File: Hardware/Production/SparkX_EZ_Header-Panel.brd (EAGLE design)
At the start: 187.2 x 136.7 mm, 1386 parts, among them J1 QWIIC_RIGHT_ANGLE, J10 QWIIC_RIGHT_ANGLE, J11 QWIIC_RIGHT_ANGLE, J12 QWIIC_RIGHT_ANGLE, J13 QWIIC_RIGHT_ANGLE, J14 QWIIC_RIGHT_ANGLE, J15 QWIIC_RIGHT_ANGLE, J16 QWIIC_RIGHT_ANGLE, J17 QWIIC_RIGHT_ANGLE, J18 QWIIC_RIGHT_ANGLE, J19 QWIIC_RIGHT_ANGLE, J2 QWIIC_RIGHT_ANGLE, J20 QWIIC_RIGHT_ANGLE, J21 QWIIC_RIGHT_ANGLE, J22 QWIIC_RIGHT_ANGLE, J23 QWIIC_RIGHT_ANGLE, J24 QWIIC_RIGHT_ANGLE, J25 QWIIC_RIGHT_ANGLE, J26 QWIIC_RIGHT_ANGLE, J27 QWIIC_RIGHT_ANGLE, J28 QWIIC_RIGHT_ANGLE, J29 QWIIC_RIGHT_ANGLE, J3 QWIIC_RIGHT_ANGLE, J30 QWIIC_RIGHT_ANGLE, J4 QWIIC_RIGHT_ANGLE, J5 QWIIC_RIGHT_ANGLE, J6 QWIIC_RIGHT_ANGLE, J7 QWIIC_RIGHT_ANGLE, J8 QWIIC_RIGHT_ANGLE, J9 QWIIC_RIGHT_ANGLE

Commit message: Add bottom silk
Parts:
- added LOGO31, LOGO32, LOGO34, LOGO35, LOGO37, LOGO38, LOGO40, LOGO41, LOGO43, LOGO44, LOGO46, LOGO47, LOGO49, LOGO50, LOGO52, LOGO53, LOGO55, LOGO56, LOGO58, LOGO59, LOGO61, LOGO62, LOGO64, LOGO65, LOGO67, LOGO68, LOGO70, LOGO71, LOGO73, LOGO74, LOGO76, LOGO77, LOGO79, LOGO80, LOGO82, LOGO83, LOGO85, LOGO86, LOGO88, LOGO89: OSHW-LOGOMINI, SparkFun-Aesthetics:OSHW-LOGO-MINI
- added LOGO33, LOGO36, LOGO39, LOGO42, LOGO45, LOGO48, LOGO51, LOGO54, LOGO57, LOGO60, LOGO63, LOGO66, LOGO69, LOGO72, LOGO75, LOGO78, LOGO81, LOGO84, LOGO87, LOGO90: QWIIC_LOGO_5MM, SparkFun-Aesthetics:QWIIC_5MM
- added U$1000, U$1019, U$1038, U$1057, U$1076, U$1095, U$1114, U$1133, U$601, U$620, U$639, U$658, U$677, U$696, U$715, U$734, U$753, U$772, U$791, U$810, U$829, U$848, U$867, U$886, U$905, U$924, U$943, U$962, U$981: (no value), output:#CIPO#0
- added U$1001, U$1020, U$1039, U$1058, U$1077, U$1096, U$1115, U$1134, U$602, U$621, U$640, U$659, U$678, U$697, U$716, U$735, U$754, U$773, U$792, U$811, U$830, U$849, U$868, U$887, U$906, U$925, U$944, U$963, U$982: (no value), output:#GPIO1#0
- added U$1002, U$1021, U$1040, U$1059, U$1078, U$1097, U$1116, U$1135, U$603, U$622, U$641, U$660, U$679, U$698, U$717, U$736, U$755, U$774, U$793, U$812, U$831, U$850, U$869, U$888, U$907, U$926, U$945, U$964, U$983: (no value), output:#CS0#0
- added U$1003, U$1022, U$1041, U$1060, U$1079, U$1098, U$1117, U$1136, U$604, U$623, U$642, U$661, U$680, U$699, U$718, U$737, U$756, U$775, U$794, U$813, U$832, U$851, U$870, U$889, U$908, U$927, U$946, U$965, U$984: (no value), output:#GPIO0#0
- added U$1004, U$1023, U$1042, U$1061, U$1080, U$1099, U$1118, U$1137, U$605, U$624, U$643, U$662, U$681, U$700, U$719, U$738, U$757, U$776, U$795, U$814, U$833, U$852, U$871, U$890, U$909, U$928, U$947, U$966, U$985: (no value), output:#CS1#0
- added U$1005, U$1024, U$1043, U$1062, U$1081, U$1100, U$1119, U$1138, U$606, U$625, U$644, U$663, U$682, U$701, U$720, U$739, U$758, U$777, U$796, U$815, U$834, U$853, U$872, U$891, U$910, U$929, U$948, U$967, U$986: (no value), output:#CS2#0
- added U$1006, U$1044, U$1082, U$1120, U$626, U$664, U$702, U$740, U$778, U$816, U$854, U$892, U$930, U$968: (no value), output:#I�C#0
- added U$1007, U$1025, U$1045, U$1063, U$1083, U$1101, U$1121, U$1139, U$607, U$627, U$645, U$665, U$683, U$703, U$721, U$741, U$759, U$779, U$797, U$817, U$835, U$855, U$873, U$893, U$911, U$931, U$949, U$969, U$987: (no value), output:EZ_HEADER0
- added U$1008, U$1026, U$1046, U$1064, U$1084, U$1102, U$1122, U$1140, U$608, U$628, U$646, U$666, U$684, U$704, U$722, U$742, U$760, U$780, U$798, U$818, U$836, U$856, U$874, U$894, U$912, U$932, U$950, U$970, U$988: (no value), output:#SCL#0
- added U$1009, U$1027, U$1047, U$1065, U$1085, U$1103, U$1123, U$609, U$629, U$647, U$667, U$685, U$705, U$723, U$743, U$761, U$781, U$799, U$819, U$837, U$857, U$875, U$895, U$913, U$933, U$951, U$971, U$989: SPARKX-LOGO3, SparkX:SPARKX-SMALL
- added U$1010, U$1029, U$1048, U$1067, U$1086, U$1105, U$1124, U$611, U$630, U$649, U$668, U$687, U$706, U$725, U$744, U$763, U$782, U$801, U$820, U$839, U$858, U$877, U$896, U$915, U$934, U$953, U$972, U$991: (no value), output:#V_USB#0
- added U$1011, U$1012, U$1030, U$1031, U$1049, U$1050, U$1068, U$1069, U$1087, U$1088, U$1106, U$1107, U$1125, U$1126, U$612, U$613, U$631, U$632, U$650, U$651, U$669, U$670, U$688, U$689, U$707, U$708, U$726, U$727, U$745, U$746, U$764, U$765, U$783, U$784, U$802, U$803, U$821, U$822, U$840, U$841, U$859, U$860, U$878, U$879, U$897, U$898, U$916, U$917, U$935, U$936, U$954, U$955, U$973, U$974, U$992, U$993: (no value), output:#3#3V#0
- added U$1013, U$1032, U$1051, U$1070, U$1089, U$1108, U$1127, U$614, U$633, U$652, U$671, U$690, U$709, U$728, U$747, U$766, U$785, U$804, U$823, U$842, U$861, U$880, U$899, U$918, U$937, U$956, U$975, U$994: (no value), output:#PWR_EN#0
- added U$1014, U$1015, U$1033, U$1034, U$1052, U$1053, U$1071, U$1072, U$1090, U$1091, U$1109, U$1110, U$1128, U$1129, U$615, U$616, U$634, U$635, U$653, U$654, U$672, U$673, U$691, U$692, U$710, U$711, U$729, U$730, U$748, U$749, U$767, U$768, U$786, U$787, U$805, U$806, U$824, U$825, U$843, U$844, U$862, U$863, U$881, U$882, U$900, U$901, U$919, U$920, U$938, U$939, U$957, U$958, U$976, U$977, U$995, U$996: (no value), output:#GND#0
- added U$1016, U$1035, U$1054, U$1073, U$1092, U$1111, U$1130, U$617, U$636, U$655, U$674, U$693, U$712, U$731, U$750, U$769, U$788, U$807, U$826, U$845, U$864, U$883, U$902, U$921, U$940, U$959, U$978, U$997: (no value), output:#SCLK#0
- added U$1017, U$1036, U$1055, U$1074, U$1093, U$1112, U$1131, U$618, U$637, U$656, U$675, U$694, U$713, U$732, U$751, U$770, U$789, U$808, U$827, U$846, U$865, U$884, U$903, U$922, U$941, U$960, U$979, U$998: (no value), output:#COPI#0
- added U$1018, U$1037, U$1056, U$1075, U$1094, U$1113, U$1132, U$619, U$638, U$657, U$676, U$695, U$714, U$733, U$752, U$771, U$790, U$809, U$828, U$847, U$866, U$885, U$904, U$923, U$942, U$961, U$980, U$999: (no value), output:#SDA#0
- added U$1028, U$1066, U$1104, U$610, U$648, U$686, U$724, U$762, U$800, U$838, U$876, U$914, U$952, U$990: (no value), output:#OUT#0
- LOGO12, LOGO15, LOGO18, LOGO21, LOGO24, LOGO27, LOGO30, LOGO4, LOGO6, LOGO9: value OSHW-LOGOMINI -> QWIIC_LOGO_5MM; device SparkFun-Aesthetics:OSHW-LOGO-MINI -> SparkFun-Aesthetics:QWIIC_5MM
- U$100, U$460, U$480, U$80: device output:#SCL#0 -> output:#3#3V#0
- U$101, U$481: value SPARKX-LOGO3 -> (none); device SparkX:SPARKX-SMALL -> output:#PWR_EN#0
- U$102, U$122, U$482, U$502: device output:#OUT#0 -> output:#GND#0
- U$103, U$463, U$483, U$83: device output:#V_USB#0 -> output:#GND#0
- U$104, U$465, U$484, U$85: device output:#3#3V#0 -> output:#SCLK#0
- U$105, U$124, U$485, U$504: device output:#3#3V#0 -> output:#COPI#0
- U$106, U$486: device output:#PWR_EN#0 -> output:#SDA#0
- U$107, U$468, U$487, U$88: device output:#GND#0 -> output:#CIPO#0
- U$108, U$127, U$488, U$507: device output:#GND#0 -> output:#GPIO1#0
- U$109, U$489: device output:#SCLK#0 -> output:#CS0#0
- U$110, U$490: device output:#COPI#0 -> output:#GPIO0#0
- U$111, U$491: device output:#SDA#0 -> output:#CS1#0
- U$112, U$492: device output:#CIPO#0 -> output:#CS2#0
- U$113, U$133, U$493, U$513: device output:#GPIO1#0 -> output:EZ_HEADER0
- U$114, U$134, U$494, U$514: device output:#CS0#0 -> output:#SCL#0
- U$115, U$135, U$495, U$515: value (none) -> SPARKX-LOGO3; device output:#GPIO0#0 -> SparkX:SPARKX-SMALL
- U$116, U$496: device output:#CS1#0 -> output:#OUT#0
- U$117, U$497: device output:#CS2#0 -> output:#V_USB#0
- U$118, U$138, U$498, U$518: device output:#I�C#0 -> output:#3#3V#0
- U$119, U$479, U$499, U$99: device output:EZ_HEADER0 -> output:#3#3V#0
- U$120, U$500: device output:#SCL#0 -> output:#PWR_EN#0
- U$121, U$141, U$501, U$521: value SPARKX-LOGO3 -> (none); device SparkX:SPARKX-SMALL -> output:#GND#0
- U$123, U$503: device output:#V_USB#0 -> output:#SCLK#0
- U$125, U$144, U$505, U$524: device output:#3#3V#0 -> output:#SDA#0
- U$126, U$506: device output:#PWR_EN#0 -> output:#CIPO#0
- U$128, U$147, U$508, U$527: device output:#GND#0 -> output:#CS0#0
- U$129, U$509: device output:#SCLK#0 -> output:#GPIO0#0
- U$130, U$510: device output:#COPI#0 -> output:#CS1#0
- U$131, U$511: device output:#SDA#0 -> output:#CS2#0
- U$132, U$512: device output:#CIPO#0 -> output:#I�C#0
- U$136, U$516: device output:#CS1#0 -> output:#V_USB#0
- U$137, U$157, U$517, U$537: device output:#CS2#0 -> output:#3#3V#0
- U$139, U$519: device output:EZ_HEADER0 -> output:#PWR_EN#0
- U$140, U$160, U$520, U$540: device output:#SCL#0 -> output:#GND#0
- U$142, U$522: device output:#OUT#0 -> output:#SCLK#0
- U$143, U$523: device output:#V_USB#0 -> output:#COPI#0
- U$145, U$164, U$525, U$544: device output:#3#3V#0 -> output:#CIPO#0
- U$146, U$526: device output:#PWR_EN#0 -> output:#GPIO1#0
- U$148, U$167, U$528, U$547: device output:#GND#0 -> output:#GPIO0#0
- U$149, U$529: device output:#SCLK#0 -> output:#CS1#0
- U$150, U$530: device output:#COPI#0 -> output:#CS2#0
- U$151, U$171, U$531, U$551: device output:#SDA#0 -> output:EZ_HEADER0
- U$152, U$172, U$532, U$552: device output:#CIPO#0 -> output:#SCL#0
- U$153, U$173, U$533, U$553: value (none) -> SPARKX-LOGO3; device output:#GPIO1#0 -> SparkX:SPARKX-SMALL
- U$154, U$534: device output:#CS0#0 -> output:#OUT#0
- U$155, U$535: device output:#GPIO0#0 -> output:#V_USB#0
- U$156, U$176, U$536, U$556: device output:#CS1#0 -> output:#3#3V#0
- U$158, U$538: device output:#I�C#0 -> output:#PWR_EN#0
- U$159, U$179, U$539, U$559: device output:EZ_HEADER0 -> output:#GND#0
- U$161, U$541: value SPARKX-LOGO3 -> (none); device SparkX:SPARKX-SMALL -> output:#SCLK#0
- U$162, U$542: device output:#OUT#0 -> output:#COPI#0
- U$163, U$543: device output:#V_USB#0 -> output:#SDA#0
- U$165, U$184, U$545, U$564: device output:#3#3V#0 -> output:#GPIO1#0
- U$166, U$546: device output:#PWR_EN#0 -> output:#CS0#0
- U$168, U$187, U$548, U$567: device output:#GND#0 -> output:#CS1#0
- U$169, U$549: device output:#SCLK#0 -> output:#CS2#0
- U$170, U$550: device output:#COPI#0 -> output:#I�C#0
- U$174, U$554: device output:#CS0#0 -> output:#V_USB#0
- U$175, U$195, U$555, U$575: device output:#GPIO0#0 -> output:#3#3V#0
- U$177, U$557: device output:#CS2#0 -> output:#PWR_EN#0
- U$178, U$198, U$558, U$578: device output:#I�C#0 -> output:#GND#0
- U$180, U$560: device output:#SCL#0 -> output:#SCLK#0
- U$181, U$561: value SPARKX-LOGO3 -> (none); device SparkX:SPARKX-SMALL -> output:#COPI#0
- U$182, U$562: device output:#OUT#0 -> output:#SDA#0
- U$183, U$563: device output:#V_USB#0 -> output:#CIPO#0
- U$185, U$204, U$565, U$584: device output:#3#3V#0 -> output:#CS0#0
- U$186, U$566: device output:#PWR_EN#0 -> output:#GPIO0#0
- U$188, U$207, U$568, U$587: device output:#GND#0 -> output:#CS2#0
- U$189, U$209, U$569, U$589: device output:#SCLK#0 -> output:EZ_HEADER0
- U$190, U$210, U$570, U$590: device output:#COPI#0 -> output:#SCL#0
- U$191, U$211, U$571, U$591: value (none) -> SPARKX-LOGO3; device output:#SDA#0 -> SparkX:SPARKX-SMALL
- U$192, U$572: device output:#CIPO#0 -> output:#OUT#0
- U$193, U$573: device output:#GPIO1#0 -> output:#V_USB#0
- U$194, U$214, U$574, U$594: device output:#CS0#0 -> output:#3#3V#0
- U$196, U$576: device output:#CS1#0 -> output:#PWR_EN#0
- U$197, U$217, U$577, U$597: device output:#CS2#0 -> output:#GND#0
- U$199, U$579: device output:EZ_HEADER0 -> output:#SCLK#0
- U$200, U$580: device output:#SCL#0 -> output:#COPI#0
- U$201, U$581: value SPARKX-LOGO3 -> (none); device SparkX:SPARKX-SMALL -> output:#SDA#0
- U$202, U$582: device output:#OUT#0 -> output:#CIPO#0
- U$203, U$583: device output:#V_USB#0 -> output:#GPIO1#0
- U$205, U$224, U$585: device output:#3#3V#0 -> output:#GPIO0#0
- U$206, U$586: device output:#PWR_EN#0 -> output:#CS1#0
- U$208, U$588: device output:#GND#0 -> output:#I�C#0
- U$212, U$592: device output:#CIPO#0 -> output:#V_USB#0
- U$213, U$233, U$593: device output:#GPIO1#0 -> output:#3#3V#0
- U$215, U$595: device output:#GPIO0#0 -> output:#PWR_EN#0
- U$216, U$236, U$596: device output:#CS1#0 -> output:#GND#0
- U$218, U$598: device output:#I�C#0 -> output:#SCLK#0
- U$219, U$599: device output:EZ_HEADER0 -> output:#COPI#0
- U$22, U$402: device output:#OUT#0 -> output:#V_USB#0
- U$220, U$600: device output:#SCL#0 -> output:#SDA#0
- U$221: value SPARKX-LOGO3 -> (none); device SparkX:SPARKX-SMALL -> output:#CIPO#0
- U$222: device output:#OUT#0 -> output:#GPIO1#0
- U$223: device output:#V_USB#0 -> output:#CS0#0
- U$225, U$244: device output:#3#3V#0 -> output:#CS1#0
- U$226: device output:#PWR_EN#0 -> output:#CS2#0
- U$227, U$247: device output:#GND#0 -> output:EZ_HEADER0
- U$228, U$248: device output:#GND#0 -> output:#SCL#0
- U$229, U$249: value (none) -> SPARKX-LOGO3; device output:#SCLK#0 -> SparkX:SPARKX-SMALL
- U$23, U$403, U$423, U$43: device output:#V_USB#0 -> output:#3#3V#0
- U$230: device output:#COPI#0 -> output:#OUT#0
- U$231: device output:#SDA#0 -> output:#V_USB#0
- U$232, U$252: device output:#CIPO#0 -> output:#3#3V#0
- U$234: device output:#CS0#0 -> output:#PWR_EN#0
- U$235, U$255: device output:#GPIO0#0 -> output:#GND#0
- U$237: device output:#CS2#0 -> output:#SCLK#0
- U$238: device output:#I�C#0 -> output:#COPI#0
- U$239: device output:EZ_HEADER0 -> output:#SDA#0
- U$240: device output:#SCL#0 -> output:#CIPO#0
- U$241: value SPARKX-LOGO3 -> (none); device SparkX:SPARKX-SMALL -> output:#GPIO1#0
- U$242: device output:#OUT#0 -> output:#CS0#0
- U$243: device output:#V_USB#0 -> output:#GPIO0#0
- U$245, U$264: device output:#3#3V#0 -> output:#CS2#0
- U$246: device output:#PWR_EN#0 -> output:#I�C#0
- U$25, U$405, U$424, U$44: device output:#3#3V#0 -> output:#PWR_EN#0
- U$250: device output:#COPI#0 -> output:#V_USB#0
- U$251, U$271: device output:#SDA#0 -> output:#3#3V#0
- U$253: device output:#GPIO1#0 -> output:#PWR_EN#0
- U$254, U$274: device output:#CS0#0 -> output:#GND#0
- U$256: device output:#CS1#0 -> output:#SCLK#0
- U$257: device output:#CS2#0 -> output:#COPI#0
- U$258: device output:#I�C#0 -> output:#SDA#0
- U$259: device output:EZ_HEADER0 -> output:#CIPO#0
- U$26, U$406, U$426, U$46: device output:#PWR_EN#0 -> output:#GND#0
- U$260: device output:#SCL#0 -> output:#GPIO1#0
- U$261: value SPARKX-LOGO3 -> (none); device SparkX:SPARKX-SMALL -> output:#CS0#0
- U$262: device output:#OUT#0 -> output:#GPIO0#0
- U$263: device output:#V_USB#0 -> output:#CS1#0
- U$265, U$285: device output:#3#3V#0 -> output:EZ_HEADER0
- U$266, U$286: device output:#PWR_EN#0 -> output:#SCL#0
- U$267, U$287: value (none) -> SPARKX-LOGO3; device output:#GND#0 -> SparkX:SPARKX-SMALL
- U$268: device output:#GND#0 -> output:#OUT#0
- U$269: device output:#SCLK#0 -> output:#V_USB#0
- U$270, U$290: device output:#COPI#0 -> output:#3#3V#0
- U$272: device output:#CIPO#0 -> output:#PWR_EN#0
- U$273, U$293: device output:#GPIO1#0 -> output:#GND#0
- U$275: device output:#GPIO0#0 -> output:#SCLK#0
- U$276: device output:#CS1#0 -> output:#COPI#0
- U$277: device output:#CS2#0 -> output:#SDA#0
- U$278: device output:#I�C#0 -> output:#CIPO#0
- U$279: device output:EZ_HEADER0 -> output:#GPIO1#0
- U$28, U$408, U$427, U$47: device output:#GND#0 -> output:#SCLK#0
- U$280: device output:#SCL#0 -> output:#CS0#0
- U$281: value SPARKX-LOGO3 -> (none); device SparkX:SPARKX-SMALL -> output:#GPIO0#0
- U$282: device output:#OUT#0 -> output:#CS1#0
- U$283: device output:#V_USB#0 -> output:#CS2#0
- U$284: device output:#3#3V#0 -> output:#I�C#0
- U$288, U$307: device output:#GND#0 -> output:#V_USB#0
- U$289, U$309: device output:#SCLK#0 -> output:#3#3V#0
- U$29, U$409: device output:#SCLK#0 -> output:#COPI#0
- U$291: device output:#SDA#0 -> output:#PWR_EN#0
- U$292, U$312: device output:#CIPO#0 -> output:#GND#0
- U$294: device output:#CS0#0 -> output:#SCLK#0
- U$295: device output:#GPIO0#0 -> output:#COPI#0
- U$296: device output:#CS1#0 -> output:#SDA#0
- U$297: device output:#CS2#0 -> output:#CIPO#0
- U$298: device output:#I�C#0 -> output:#GPIO1#0
- U$299: device output:EZ_HEADER0 -> output:#CS0#0
- U$30, U$410: device output:#COPI#0 -> output:#SDA#0
- U$300: device output:#SCL#0 -> output:#GPIO0#0
- U$301: value SPARKX-LOGO3 -> (none); device SparkX:SPARKX-SMALL -> output:#CS1#0
- U$302: device output:#OUT#0 -> output:#CS2#0
- U$303, U$323: device output:#V_USB#0 -> output:EZ_HEADER0
- U$304, U$324: device output:#3#3V#0 -> output:#SCL#0
- U$305, U$325: value (none) -> SPARKX-LOGO3; device output:#3#3V#0 -> SparkX:SPARKX-SMALL
- U$306: device output:#PWR_EN#0 -> output:#OUT#0
- U$308, U$327, U$328, U$347: device output:#GND#0 -> output:#3#3V#0
- U$31, U$411: device output:#SDA#0 -> output:#CIPO#0
- U$310: device output:#COPI#0 -> output:#PWR_EN#0
- U$311, U$331: device output:#SDA#0 -> output:#GND#0
- U$313: device output:#GPIO1#0 -> output:#SCLK#0
- U$314: device output:#CS0#0 -> output:#COPI#0
- U$315: device output:#GPIO0#0 -> output:#SDA#0
- U$316: device output:#CS1#0 -> output:#CIPO#0
- U$317: device output:#CS2#0 -> output:#GPIO1#0
- U$318: device output:#I�C#0 -> output:#CS0#0
- U$319: device output:EZ_HEADER0 -> output:#GPIO0#0
- U$32, U$412: device output:#CIPO#0 -> output:#GPIO1#0
- U$320: device output:#SCL#0 -> output:#CS1#0
- U$321: value SPARKX-LOGO3 -> (none); device SparkX:SPARKX-SMALL -> output:#CS2#0
- U$322: device output:#OUT#0 -> output:#I�C#0
- U$326: device output:#PWR_EN#0 -> output:#V_USB#0
- U$329: device output:#SCLK#0 -> output:#PWR_EN#0
- U$33, U$413: device output:#GPIO1#0 -> output:#CS0#0
- U$330, U$350: device output:#COPI#0 -> output:#GND#0
- U$332: device output:#CIPO#0 -> output:#SCLK#0
- U$333: device output:#GPIO1#0 -> output:#COPI#0
- U$334: device output:#CS0#0 -> output:#SDA#0
- U$335: device output:#GPIO0#0 -> output:#CIPO#0
- U$336: device output:#CS1#0 -> output:#GPIO1#0
- U$337: device output:#CS2#0 -> output:#CS0#0
- U$338: device output:#I�C#0 -> output:#GPIO0#0
- U$339: device output:EZ_HEADER0 -> output:#CS1#0
- U$34, U$414: device output:#CS0#0 -> output:#GPIO0#0
- U$340: device output:#SCL#0 -> output:#CS2#0
- U$341, U$361: value SPARKX-LOGO3 -> (none); device SparkX:SPARKX-SMALL -> output:EZ_HEADER0
- U$342, U$362: device output:#OUT#0 -> output:#SCL#0
- U$343, U$363: value (none) -> SPARKX-LOGO3; device output:#V_USB#0 -> SparkX:SPARKX-SMALL
- U$344: device output:#3#3V#0 -> output:#OUT#0
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
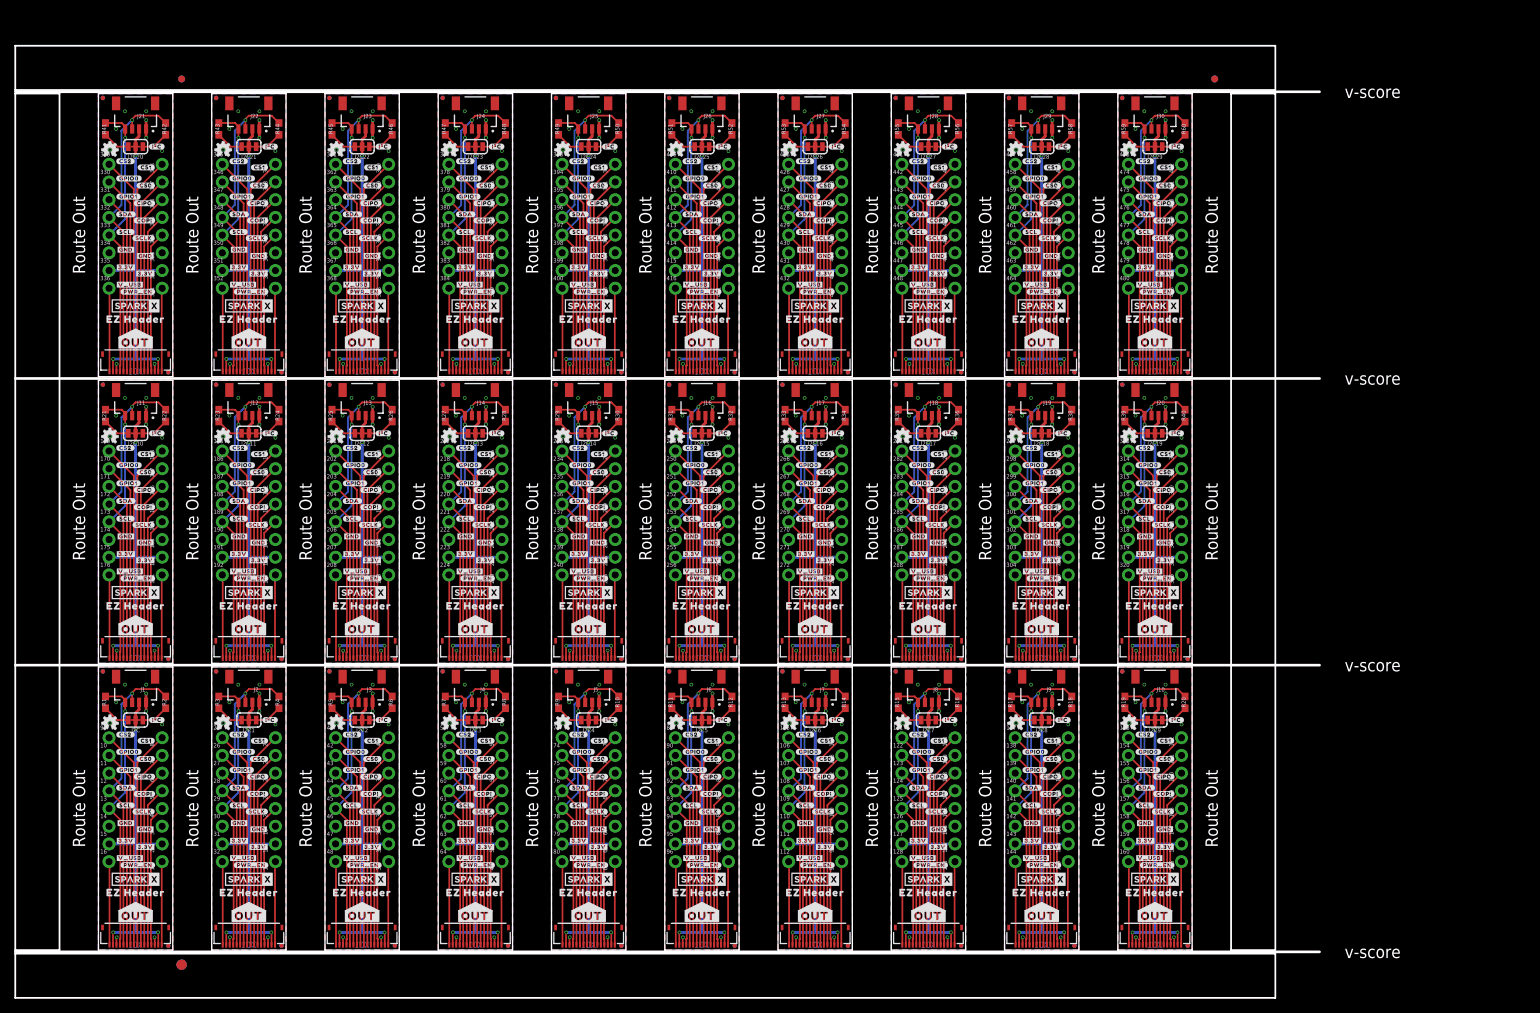
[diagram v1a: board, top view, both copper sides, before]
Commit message: Gapless production panel
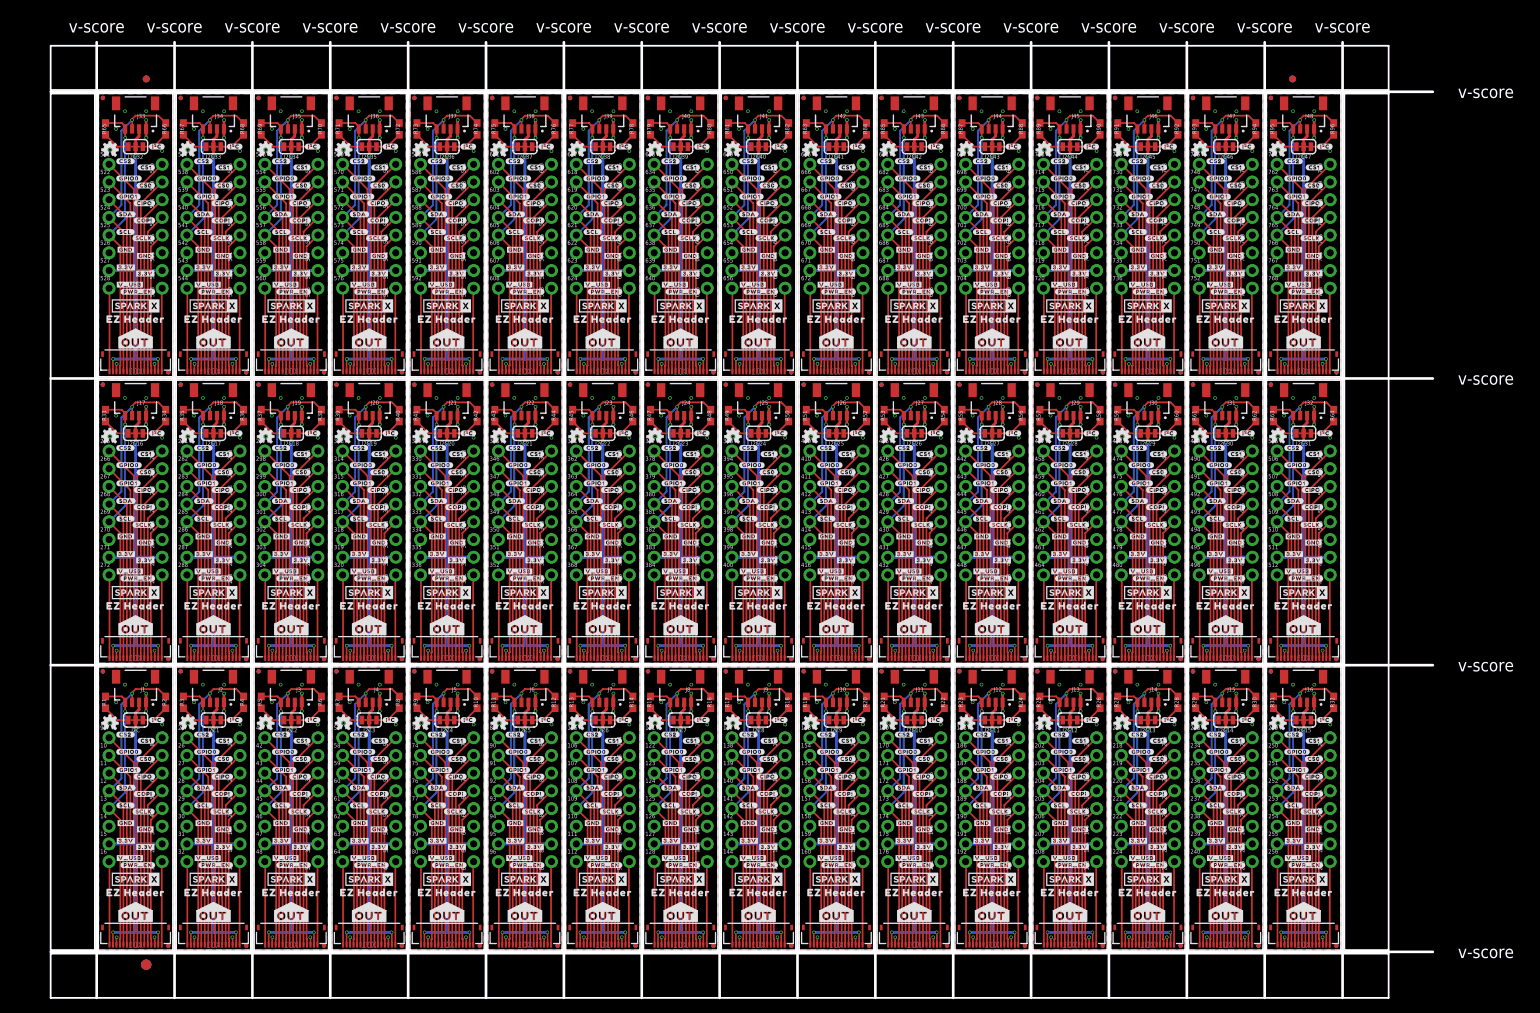
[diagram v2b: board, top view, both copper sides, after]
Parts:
- added 481, 482, 483, 484, 485, 486, 487, 488, 489, 490, 491, 492, 493, 494, 495, 496, 497, 498, 499, 500, 501, 502, 503, 504, 505, 506, 507, 508, 509, 510, 511, 512, 513, 514, 515, 516, 517, 518, 519, 520, 521, 522, 523, 524, 525, 526, 527, 528, 529, 530, 531, 532, 533, 534, 535, 536, 537, 538, 539, 540, 541, 542, 543, 544, 545, 546, 547, 548, 549, 550, 551, 552, 553, 554, 555, 556, 557, 558, 559, 560, 561, 562, 563, 564, 565, 566, 567, 568, 569, 570, 571, 572, 573, 574, 575, 576, 577, 578, 579, 580, 581, 582, 583, 584, 585, 586, 587, 588, 589, 590, 591, 592, 593, 594, 595, 596, 597, 598, 599, 600, 601, 602, 603, 604, 605, 606, 607, 608, 609, 610, 611, 612, 613, 614, 615, 616, 617, 618, 619, 620, 621, 622, 623, 624, 625, 626, 627, 628, 629, 630, 631, 632, 633, 634, 635, 636, 637, 638, 639, 640, 641, 642, 643, 644, 645, 646, 647, 648, 649, 650, 651, 652, 653, 654, 655, 656, 657, 658, 659, 660, 661, 662, 663, 664, 665, 666, 667, 668, 669, 670, 671, 672, 673, 674, 675, 676, 677, 678, 679, 680, 681, 682, 683, 684, 685, 686, 687, 688, 689, 690, 691, 692, 693, 694, 695, 696, 697, 698, 699, 700, 701, 702, 703, 704, 705, 706, 707, 708, 709, 710, 711, 712, 713, 714, 715, 716, 717, 718, 719, 720, 721, 722, 723, 724, 725, 726, 727, 728, 729, 730, 731, 732, 733, 734, 735, 736, 737, 738, 739, 740, 741, 742, 743, 744, 745, 746, 747, 748, 749, 750, 751, 752, 753, 754, 755, 756, 757, 758, 759, 760, 761, 762, 763, 764, 765, 766, 767, 768: (no value), SparkFun-Connectors:1X01_NO_SILK
- added FD121, FD122, FD123, FD124, FD125, FD126, FD127, FD128, FD129, FD130, FD131, FD132, FD133, FD134, FD135, FD136, FD137, FD138, FD139, FD140, FD141, FD142, FD143, FD144, FD145, FD146, FD147, FD148, FD149, FD150, FD151, FD152, FD153, FD154, FD155, FD156, FD157, FD158, FD159, FD160, FD161, FD162, FD163, FD164, FD165, FD166, FD167, FD168, FD169, FD170, FD171, FD172, FD173, FD174, FD175, FD176, FD177, FD178, FD179, FD180, FD181, FD182, FD183, FD184, FD185, FD186, FD187, FD188, FD189, FD190, FD191, FD192: FIDUCIALUFIDUCIAL, SparkFun-Aesthetics:FIDUCIAL-MICRO
- added I2C30, I2C31, I2C32, I2C33, I2C34, I2C35, I2C36, I2C37, I2C38, I2C39, I2C40, I2C41, I2C42, I2C43, I2C44, I2C45, I2C46, I2C47: JUMPER-SMT_3_2-NC_TRACE_SILK, SparkFun-Jumpers:SMT-JUMPER_3_2-NC_TRACE_SILK
- added J31, J32, J33, J34, J35, J36, J37, J38, J39, J40, J41, J42, J43, J44, J45, J46, J47, J48: QWIIC_RIGHT_ANGLE, SparkFun-Connectors:JST04_1MM_RA
- added LOGO100, LOGO101, LOGO103, LOGO104, LOGO106, LOGO107, LOGO109, LOGO110, LOGO112, LOGO113, LOGO115, LOGO116, LOGO118, LOGO119, LOGO121, LOGO122, LOGO124, LOGO125, LOGO127, LOGO128, LOGO130, LOGO131, LOGO133, LOGO134, LOGO136, LOGO137, LOGO139, LOGO140, LOGO142, LOGO143, LOGO91, LOGO92, LOGO94, LOGO95, LOGO97, LOGO98: OSHW-LOGOMINI, SparkFun-Aesthetics:OSHW-LOGO-MINI
- added LOGO102, LOGO105, LOGO108, LOGO111, LOGO114, LOGO117, LOGO120, LOGO123, LOGO126, LOGO129, LOGO132, LOGO135, LOGO138, LOGO141, LOGO144, LOGO93, LOGO96, LOGO99: QWIIC_LOGO_5MM, SparkFun-Aesthetics:QWIIC_5MM
- added OUT30, OUT31, OUT32, OUT33, OUT34, OUT35, OUT36, OUT37, OUT38, OUT39, OUT40, OUT41, OUT42, OUT43, OUT44, OUT45, OUT46, OUT47: FPC_16_0.5MM_BACKFLIP, New_Parts_Connectors:FPC_16_DOUBLESIDED_BACKFLIP
- added R61, R62, R63, R64, R65, R66, R67, R68, R69, R70, R71, R72, R73, R74, R75, R76, R77, R78, R79, R80, R81, R82, R83, R84, R85, R86, R87, R88, R89, R90, R91, R92, R93, R94, R95, R96: 2.2k, SparkFun-Resistors:0603
- added U$1141, U$1161, U$1179, U$1199, U$1217, U$1237, U$1255, U$1275, U$1293, U$1313, U$1331, U$1351, U$1369, U$1389, U$1407, U$1427, U$1445, U$1465, U$1483, U$1503, U$1521, U$1541, U$1559, U$1579, U$1597, U$1617, U$1635, U$1655, U$1673, U$1693, U$1711, U$1731, U$1749, U$1769, U$1787, U$1807: SPARKX-LOGO3, SparkX:SPARKX-SMALL
- added U$1142, U$1180, U$1218, U$1256, U$1294, U$1332, U$1370, U$1408, U$1446, U$1484, U$1522, U$1560, U$1598, U$1636, U$1674, U$1712, U$1750, U$1788: (no value), output:#OUT#0
- added U$1143, U$1162, U$1181, U$1200, U$1219, U$1238, U$1257, U$1276, U$1295, U$1314, U$1333, U$1352, U$1371, U$1390, U$1409, U$1428, U$1447, U$1466, U$1485, U$1504, U$1523, U$1542, U$1561, U$1580, U$1599, U$1618, U$1637, U$1656, U$1675, U$1694, U$1713, U$1732, U$1751, U$1770, U$1789, U$1808: (no value), output:#V_USB#0
- added U$1144, U$1145, U$1163, U$1164, U$1182, U$1183, U$1201, U$1202, U$1220, U$1221, U$1239, U$1240, U$1258, U$1259, U$1277, U$1278, U$1296, U$1297, U$1315, U$1316, U$1334, U$1335, U$1353, U$1354, U$1372, U$1373, U$1391, U$1392, U$1410, U$1411, U$1429, U$1430, U$1448, U$1449, U$1467, U$1468, U$1486, U$1487, U$1505, U$1506, U$1524, U$1525, U$1543, U$1544, U$1562, U$1563, U$1581, U$1582, U$1600, U$1601, U$1619, U$1620, U$1638, U$1639, U$1657, U$1658, U$1676, U$1677, U$1695, U$1696, U$1714, U$1715, U$1733, U$1734, U$1752, U$1753, U$1771, U$1772, U$1790, U$1791, U$1809, U$1810: (no value), output:#3#3V#0
- added U$1146, U$1165, U$1184, U$1203, U$1222, U$1241, U$1260, U$1279, U$1298, U$1317, U$1336, U$1355, U$1374, U$1393, U$1412, U$1431, U$1450, U$1469, U$1488, U$1507, U$1526, U$1545, U$1564, U$1583, U$1602, U$1621, U$1640, U$1659, U$1678, U$1697, U$1716, U$1735, U$1754, U$1773, U$1792, U$1811: (no value), output:#PWR_EN#0
- added U$1147, U$1148, U$1166, U$1167, U$1185, U$1186, U$1204, U$1205, U$1223, U$1224, U$1242, U$1243, U$1261, U$1262, U$1280, U$1281, U$1299, U$1300, U$1318, U$1319, U$1337, U$1338, U$1356, U$1357, U$1375, U$1376, U$1394, U$1395, U$1413, U$1414, U$1432, U$1433, U$1451, U$1452, U$1470, U$1471, U$1489, U$1490, U$1508, U$1509, U$1527, U$1528, U$1546, U$1547, U$1565, U$1566, U$1584, U$1585, U$1603, U$1604, U$1622, U$1623, U$1641, U$1642, U$1660, U$1661, U$1679, U$1680, U$1698, U$1699, U$1717, U$1718, U$1736, U$1737, U$1755, U$1756, U$1774, U$1775, U$1793, U$1794, U$1812, U$1813: (no value), output:#GND#0
- added U$1149, U$1168, U$1187, U$1206, U$1225, U$1244, U$1263, U$1282, U$1301, U$1320, U$1339, U$1358, U$1377, U$1396, U$1415, U$1434, U$1453, U$1472, U$1491, U$1510, U$1529, U$1548, U$1567, U$1586, U$1605, U$1624, U$1643, U$1662, U$1681, U$1700, U$1719, U$1738, U$1757, U$1776, U$1795, U$1814: (no value), output:#SCLK#0
- added U$1150, U$1169, U$1188, U$1207, U$1226, U$1245, U$1264, U$1283, U$1302, U$1321, U$1340, U$1359, U$1378, U$1397, U$1416, U$1435, U$1454, U$1473, U$1492, U$1511, U$1530, U$1549, U$1568, U$1587, U$1606, U$1625, U$1644, U$1663, U$1682, U$1701, U$1720, U$1739, U$1758, U$1777, U$1796, U$1815: (no value), output:#COPI#0
- added U$1151, U$1170, U$1189, U$1208, U$1227, U$1246, U$1265, U$1284, U$1303, U$1322, U$1341, U$1360, U$1379, U$1398, U$1417, U$1436, U$1455, U$1474, U$1493, U$1512, U$1531, U$1550, U$1569, U$1588, U$1607, U$1626, U$1645, U$1664, U$1683, U$1702, U$1721, U$1740, U$1759, U$1778, U$1797, U$1816: (no value), output:#SDA#0
- added U$1152, U$1171, U$1190, U$1209, U$1228, U$1247, U$1266, U$1285, U$1304, U$1323, U$1342, U$1361, U$1380, U$1399, U$1418, U$1437, U$1456, U$1475, U$1494, U$1513, U$1532, U$1551, U$1570, U$1589, U$1608, U$1627, U$1646, U$1665, U$1684, U$1703, U$1722, U$1741, U$1760, U$1779, U$1798, U$1817: (no value), output:#CIPO#0
- added U$1153, U$1172, U$1191, U$1210, U$1229, U$1248, U$1267, U$1286, U$1305, U$1324, U$1343, U$1362, U$1381, U$1400, U$1419, U$1438, U$1457, U$1476, U$1495, U$1514, U$1533, U$1552, U$1571, U$1590, U$1609, U$1628, U$1647, U$1666, U$1685, U$1704, U$1723, U$1742, U$1761, U$1780, U$1799, U$1818: (no value), output:#GPIO1#0
- added U$1154, U$1173, U$1192, U$1211, U$1230, U$1249, U$1268, U$1287, U$1306, U$1325, U$1344, U$1363, U$1382, U$1401, U$1420, U$1439, U$1458, U$1477, U$1496, U$1515, U$1534, U$1553, U$1572, U$1591, U$1610, U$1629, U$1648, U$1667, U$1686, U$1705, U$1724, U$1743, U$1762, U$1781, U$1800, U$1819: (no value), output:#CS0#0
- added U$1155, U$1174, U$1193, U$1212, U$1231, U$1250, U$1269, U$1288, U$1307, U$1326, U$1345, U$1364, U$1383, U$1402, U$1421, U$1440, U$1459, U$1478, U$1497, U$1516, U$1535, U$1554, U$1573, U$1592, U$1611, U$1630, U$1649, U$1668, U$1687, U$1706, U$1725, U$1744, U$1763, U$1782, U$1801, U$1820: (no value), output:#GPIO0#0
- added U$1156, U$1175, U$1194, U$1213, U$1232, U$1251, U$1270, U$1289, U$1308, U$1327, U$1346, U$1365, U$1384, U$1403, U$1422, U$1441, U$1460, U$1479, U$1498, U$1517, U$1536, U$1555, U$1574, U$1593, U$1612, U$1631, U$1650, U$1669, U$1688, U$1707, U$1726, U$1745, U$1764, U$1783, U$1802, U$1821: (no value), output:#CS1#0
- added U$1157, U$1176, U$1195, U$1214, U$1233, U$1252, U$1271, U$1290, U$1309, U$1328, U$1347, U$1366, U$1385, U$1404, U$1423, U$1442, U$1461, U$1480, U$1499, U$1518, U$1537, U$1556, U$1575, U$1594, U$1613, U$1632, U$1651, U$1670, U$1689, U$1708, U$1727, U$1746, U$1765, U$1784, U$1803, U$1822: (no value), output:#CS2#0
- added U$1158, U$1196, U$1234, U$1272, U$1310, U$1348, U$1386, U$1424, U$1462, U$1500, U$1538, U$1576, U$1614, U$1652, U$1690, U$1728, U$1766, U$1804: (no value), output:#I�C#0
- added U$1159, U$1177, U$1197, U$1215, U$1235, U$1253, U$1273, U$1291, U$1311, U$1329, U$1349, U$1367, U$1387, U$1405, U$1425, U$1443, U$1463, U$1481, U$1501, U$1519, U$1539, U$1557, U$1577, U$1595, U$1615, U$1633, U$1653, U$1671, U$1691, U$1709, U$1729, U$1747, U$1767, U$1785, U$1805, U$1823: (no value), output:EZ_HEADER0
- added U$1160, U$1178, U$1198, U$1216, U$1236, U$1254, U$1274, U$1292, U$1312, U$1330, U$1350, U$1368, U$1388, U$1406, U$1426, U$1444, U$1464, U$1482, U$1502, U$1520, U$1540, U$1558, U$1578, U$1596, U$1616, U$1634, U$1654, U$1672, U$1692, U$1710, U$1730, U$1748, U$1768, U$1786, U$1806, U$1824: (no value), output:#SCL#0
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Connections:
- new net 3.3V30: 482.1, 495.1, I2C30.2, J31.2, OUT30.15, OUT30.2
- new net 3.3V31: 498.1, 511.1, I2C31.2, J32.2, OUT31.15, OUT31.2
- new net 3.3V32: 514.1, 527.1, I2C32.2, J33.2, OUT32.15, OUT32.2
- new net 3.3V33: 530.1, 543.1, I2C33.2, J34.2, OUT33.15, OUT33.2
- new net 3.3V34: 546.1, 559.1, I2C34.2, J35.2, OUT34.15, OUT34.2
- new net 3.3V35: 562.1, 575.1, I2C35.2, J36.2, OUT35.15, OUT35.2
- new net 3.3V36: 578.1, 591.1, I2C36.2, J37.2, OUT36.15, OUT36.2
- new net 3.3V37: 594.1, 607.1, I2C37.2, J38.2, OUT37.15, OUT37.2
- new net 3.3V38: 610.1, 623.1, I2C38.2, J39.2, OUT38.15, OUT38.2
- new net 3.3V39: 626.1, 639.1, I2C39.2, J40.2, OUT39.15, OUT39.2
- new net 3.3V40: 642.1, 655.1, I2C40.2, J41.2, OUT40.15, OUT40.2
- new net 3.3V41: 658.1, 671.1, I2C41.2, J42.2, OUT41.15, OUT41.2
- new net 3.3V42: 674.1, 687.1, I2C42.2, J43.2, OUT42.15, OUT42.2
- new net 3.3V43: 690.1, 703.1, I2C43.2, J44.2, OUT43.15, OUT43.2
- new net 3.3V44: 706.1, 719.1, I2C44.2, J45.2, OUT44.15, OUT44.2
- new net 3.3V45: 722.1, 735.1, I2C45.2, J46.2, OUT45.15, OUT45.2
- new net 3.3V46: 738.1, 751.1, I2C46.2, J47.2, OUT46.15, OUT46.2
- new net 3.3V47: 754.1, 767.1, I2C47.2, J48.2, OUT47.15, OUT47.2
- new net CIPO30: 486.1, OUT30.6
- new net CIPO31: 502.1, OUT31.6
- new net CIPO32: 518.1, OUT32.6
- new net CIPO33: 534.1, OUT33.6
- new net CIPO34: 550.1, OUT34.6
- new net CIPO35: 566.1, OUT35.6
- new net CIPO36: 582.1, OUT36.6
- new net CIPO37: 598.1, OUT37.6
- new net CIPO38: 614.1, OUT38.6
- new net CIPO39: 630.1, OUT39.6
- new net CIPO40: 646.1, OUT40.6
- new net CIPO41: 662.1, OUT41.6
- new net CIPO42: 678.1, OUT42.6
- new net CIPO43: 694.1, OUT43.6
- new net CIPO44: 710.1, OUT44.6
- new net CIPO45: 726.1, OUT45.6
- new net CIPO46: 742.1, OUT46.6
- new net CIPO47: 758.1, OUT47.6
- new net COPI30: 485.1, OUT30.5
- new net COPI31: 501.1, OUT31.5
- new net COPI32: 517.1, OUT32.5
- new net COPI33: 533.1, OUT33.5
- new net COPI34: 549.1, OUT34.5
- new net COPI35: 565.1, OUT35.5
- new net COPI36: 581.1, OUT36.5
- new net COPI37: 597.1, OUT37.5
- new net COPI38: 613.1, OUT38.5
- new net COPI39: 629.1, OUT39.5
- new net COPI40: 645.1, OUT40.5
- new net COPI41: 661.1, OUT41.5
- new net COPI42: 677.1, OUT42.5
- new net COPI43: 693.1, OUT43.5
- new net COPI44: 709.1, OUT44.5
- new net COPI45: 725.1, OUT45.5
- new net COPI46: 741.1, OUT46.5
- new net COPI47: 757.1, OUT47.5
- new net CS100: 536.1, OUT33.8
- new net CS101: 537.1, OUT33.9
- new net CS102: 551.1, OUT34.7
- new net CS103: 552.1, OUT34.8
- new net CS104: 553.1, OUT34.9
- new net CS105: 567.1, OUT35.7
- new net CS106: 568.1, OUT35.8
- new net CS107: 569.1, OUT35.9
- new net CS108: 583.1, OUT36.7
- new net CS109: 584.1, OUT36.8
- new net CS110: 585.1, OUT36.9
- new net CS111: 599.1, OUT37.7
- new net CS112: 600.1, OUT37.8
- new net CS113: 601.1, OUT37.9
- new net CS114: 615.1, OUT38.7
- new net CS115: 616.1, OUT38.8
- new net CS116: 617.1, OUT38.9
- new net CS117: 631.1, OUT39.7
- new net CS118: 632.1, OUT39.8
- new net CS119: 633.1, OUT39.9
- new net CS120: 647.1, OUT40.7
- new net CS121: 648.1, OUT40.8
- new net CS122: 649.1, OUT40.9
- new net CS123: 663.1, OUT41.7
- new net CS124: 664.1, OUT41.8
- new net CS125: 665.1, OUT41.9
- new net CS126: 679.1, OUT42.7
- new net CS127: 680.1, OUT42.8
- new net CS128: 681.1, OUT42.9
- new net CS129: 695.1, OUT43.7
- new net CS130: 696.1, OUT43.8
- new net CS131: 697.1, OUT43.9
- new net CS132: 711.1, OUT44.7
- new net CS133: 712.1, OUT44.8
- new net CS134: 713.1, OUT44.9
- new net CS135: 727.1, OUT45.7
- new net CS136: 728.1, OUT45.8
- new net CS137: 729.1, OUT45.9
- new net CS138: 743.1, OUT46.7
- new net CS139: 744.1, OUT46.8
- new net CS140: 745.1, OUT46.9
- new net CS141: 759.1, OUT47.7
- new net CS142: 760.1, OUT47.8
- new net CS143: 761.1, OUT47.9
- new net CS90: 487.1, OUT30.7
- new net CS91: 488.1, OUT30.8
- new net CS92: 489.1, OUT30.9
- new net CS93: 503.1, OUT31.7
- new net CS94: 504.1, OUT31.8
- new net CS95: 505.1, OUT31.9
- new net CS96: 519.1, OUT32.7
- new net CS97: 520.1, OUT32.8
- new net CS98: 521.1, OUT32.9
- new net CS99: 535.1, OUT33.7
- new net GND30: 483.1, 494.1, J31.1, OUT30.14, OUT30.3
- new net GND31: 499.1, 510.1, J32.1, OUT31.14, OUT31.3
- new net GND32: 515.1, 526.1, J33.1, OUT32.14, OUT32.3
- new net GND33: 531.1, 542.1, J34.1, OUT33.14, OUT33.3
- new net GND34: 547.1, 558.1, J35.1, OUT34.14, OUT34.3
- new net GND35: 563.1, 574.1, J36.1, OUT35.14, OUT35.3
- new net GND36: 579.1, 590.1, J37.1, OUT36.14, OUT36.3
- new net GND37: 595.1, 606.1, J38.1, OUT37.14, OUT37.3
- new net GND38: 611.1, 622.1, J39.1, OUT38.14, OUT38.3
- new net GND39: 627.1, 638.1, J40.1, OUT39.14, OUT39.3
- new net GND40: 643.1, 654.1, J41.1, OUT40.14, OUT40.3
- new net GND41: 659.1, 670.1, J42.1, OUT41.14, OUT41.3
- new net GND42: 675.1, 686.1, J43.1, OUT42.14, OUT42.3
- new net GND43: 691.1, 702.1, J44.1, OUT43.14, OUT43.3
- new net GND44: 707.1, 718.1, J45.1, OUT44.14, OUT44.3
- new net GND45: 723.1, 734.1, J46.1, OUT45.14, OUT45.3
- new net GND46: 739.1, 750.1, J47.1, OUT46.14, OUT46.3
- new net GND47: 755.1, 766.1, J48.1, OUT47.14, OUT47.3
- new net GPIO60: 490.1, OUT30.10
- new net GPIO61: 491.1, OUT30.11
- new net GPIO62: 506.1, OUT31.10
- new net GPIO63: 507.1, OUT31.11
- new net GPIO64: 522.1, OUT32.10
- new net GPIO65: 523.1, OUT32.11
- new net GPIO66: 538.1, OUT33.10
- new net GPIO67: 539.1, OUT33.11
- new net GPIO68: 554.1, OUT34.10
- new net GPIO69: 555.1, OUT34.11
- new net GPIO70: 570.1, OUT35.10
- new net GPIO71: 571.1, OUT35.11
- new net GPIO72: 586.1, OUT36.10
- new net GPIO73: 587.1, OUT36.11
- new net GPIO74: 602.1, OUT37.10
- new net GPIO75: 603.1, OUT37.11
- new net GPIO76: 618.1, OUT38.10
- new net GPIO77: 619.1, OUT38.11
- new net GPIO78: 634.1, OUT39.10
- new net GPIO79: 635.1, OUT39.11
- new net GPIO80: 650.1, OUT40.10
- new net GPIO81: 651.1, OUT40.11
- new net GPIO82: 666.1, OUT41.10
- new net GPIO83: 667.1, OUT41.11
- new net GPIO84: 682.1, OUT42.10
- new net GPIO85: 683.1, OUT42.11
- new net GPIO86: 698.1, OUT43.10
- new net GPIO87: 699.1, OUT43.11
- new net GPIO88: 714.1, OUT44.10
- new net GPIO89: 715.1, OUT44.11
- new net GPIO90: 730.1, OUT45.10
- new net GPIO91: 731.1, OUT45.11
- new net GPIO92: 746.1, OUT46.10
- new net GPIO93: 747.1, OUT46.11
- new net GPIO94: 762.1, OUT47.10
- new net GPIO95: 763.1, OUT47.11
- new net N$61: I2C30.3, R61.2
- new net N$62: I2C30.1, R62.2
- new net N$63: I2C31.3, R63.2
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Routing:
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- added copper zone on layer 1, net GND30
- added copper zone on layer 16, net GND30
- added copper zone on layer 1, net GND31
- added copper zone on layer 16, net GND31
- added copper zone on layer 1, net GND32
- added copper zone on layer 16, net GND32
- added copper zone on layer 1, net GND33
- added copper zone on layer 16, net GND33
- added copper zone on layer 1, net GND34
- added copper zone on layer 16, net GND34
- added copper zone on layer 1, net GND35
- added copper zone on layer 16, net GND35
- added copper zone on layer 1, net GND36
- added copper zone on layer 16, net GND36
- added copper zone on layer 1, net GND37
- added copper zone on layer 16, net GND37
- added copper zone on layer 1, net GND38
- added copper zone on layer 16, net GND38
- added copper zone on layer 1, net GND39
- added copper zone on layer 16, net GND39
- added copper zone on layer 1, net GND40
- added copper zone on layer 16, net GND40
- added copper zone on layer 1, net GND41
- added copper zone on layer 16, net GND41
- added copper zone on layer 1, net GND42
- added copper zone on layer 16, net GND42
- added copper zone on layer 1, net GND43
- added copper zone on layer 16, net GND43
- added copper zone on layer 1, net GND44
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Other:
- board size 187.2 x 136.7 mm -> 198.4 x 137.2 mm
- board text removed: "Route Out"
